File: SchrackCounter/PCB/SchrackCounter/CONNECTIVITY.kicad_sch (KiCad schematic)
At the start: 13 parts, among them J2 TYPE-C-31-M-12 (USB C CONN), U7 USBLC6-2SC6

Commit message: PCB layout update
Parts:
- added D_EXT1, D_EXT2, D_EXT3: Conn_01x02_Pin, Connector_JST:JST_XH_B2B-XH-A_1x02_P2.50mm_Vertical, symbol Connector:Conn_01x02_Pin
- added R2, R3, R4: 220R, Resistor_SMD:R_0805_2012Metric_Pad1.20x1.40mm_HandSolder, symbol Device:R
- added R5: 0R, Resistor_SMD:R_0805_2012Metric_Pad1.20x1.40mm_HandSolder, symbol Device:R
- renumbered D4 to D2, D5 to D3, D2 to D4, D3 to D5, R3 to R6, R4 to R7, R5 to R8, R2 to R9
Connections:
- net BZ1_PWM: now also R5.1; no longer BZ1.1 (+)
- net GND: now also D_EXT1.2 (Pin_2), D_EXT2.2 (Pin_2), D_EXT3.2 (Pin_2)
- new net: D_EXT1.1 (Pin_1), R2.1
- new net: BZ1.1 (+), R5.2
- new net: D_EXT3.1 (Pin_1), R4.1
- new net: D_EXT2.1 (Pin_1), R3.1
- new net LED_EXT1: R2.2
- new net LED_EXT2: R3.2
- new net LED_EXT3: R4.2
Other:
- note added: "EXTERNAL LEDS"
- note added: "LEDS/BUZZER"
- note removed: "SIGNALING"
- moved on the sheet: BZ1, D2, D3, D4, D5, R8, R9

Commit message: bom final, schematic updates
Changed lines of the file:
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@@
 		(dnp no)
 		(property "Reference" "R2"
-			(at 81.915 113.665 90)
+			(at 81.28 113.792 90)
 			(effects
 				(font
@@
 		(dnp no)
 		(property "Reference" "R3"
-			(at 81.915 126.365 90)
+			(at 81.28 126.492 90)
 			(effects
 				(font
@@
 		(dnp no)
 		(property "Reference" "R4"
-			(at 81.915 137.795 90)
-			(effects
-				(font
+			(at 81.28 137.922 90)
+			(effects
+				(font

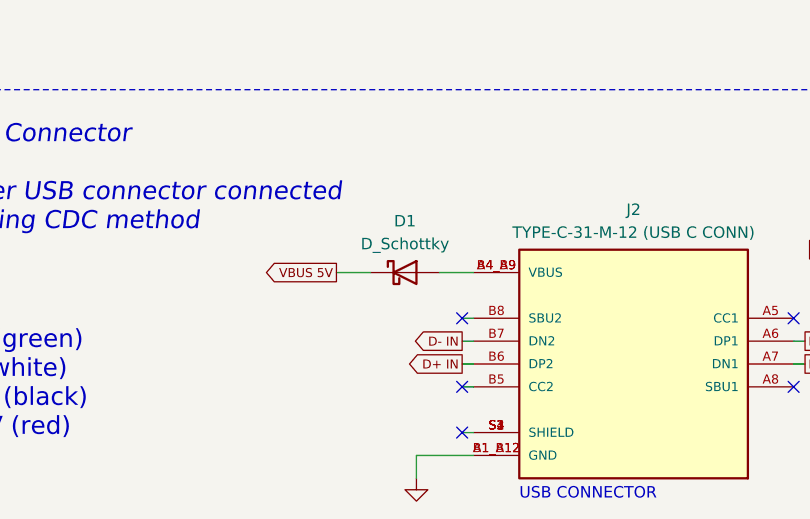
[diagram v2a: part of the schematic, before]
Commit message: PCB update, minor schematic update
PCB routing update, 7segment routing, and minor changes to the 7segments in schematic
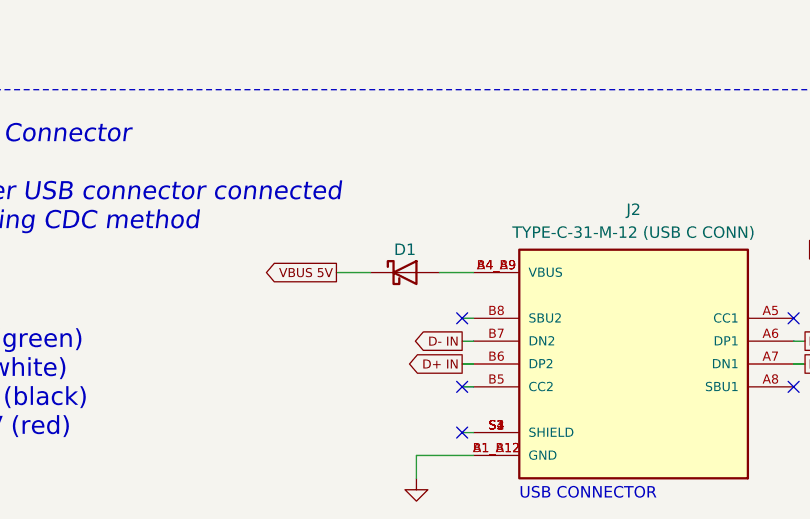
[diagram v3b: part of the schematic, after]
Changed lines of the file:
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@@
 		(effects
 			(font
+				(face "Bahnschrift")
 				(size 2 2)
 				(italic yes)
@@
 		(effects
 			(font
+				(face "Bahnschrift")
 				(size 5 5)
 				(thickness 1.2)
@@
 		(effects
 			(font
+				(face "Bahnschrift")
 				(size 5 5)
 				(thickness 1.2)
@@
 		(dnp no)
 		(property "Reference" "D1"
-			(at 120.65 46.355 0)
+			(at 120.65 49.53 0)
 			(effects
 				(font
@@
 					(size 1.27 1.27)
 				)
-			)
-		)
+				(hide yes)
+			)
+		)

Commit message: SchrackCounter
PCB Finished
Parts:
- renumbered D5 to D4, D4 to D5
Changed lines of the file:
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@@
 	(wire
 		(pts
-			(xy 124.46 52.07) (xy 128.27 52.07)
+			(xy 123.19 52.07) (xy 128.27 52.07)
 		)
 		(stroke
@@
 	(wire
 		(pts
-			(xy 113.03 52.07) (xy 116.84 52.07)
+			(xy 107.95 52.07) (xy 115.57 52.07)
 		)
 		(stroke
@@
 	(global_label "VBUS 5V"
 		(shape output)
-		(at 113.03 52.07 180)
+		(at 107.95 52.07 180)
 		(fields_autoplaced yes)
 		(effects
@@
 		)
 		(property "Intersheetrefs" "${INTERSHEET_REFS}"
-			(at 105.4326 52.07 0)
+			(at 100.3526 52.07 0)
 			(effects
 				(font
@@
 		(dnp no)
 		(fields_autoplaced yes)
-		(property "Reference" "#PWR023"
+		(property "Reference" "#PWR022"
 			(at 173.99 62.23 0)
 			(effects
@@
 			(project "SchrackCounter"
 				(path "/d96f2ffc-3f4c-4f71-b693-29f6b8c3245d/301b3ab9-8372-40d2-93c7-cd7607d23fc4"
-					(reference "#PWR023")
+					(reference "#PWR022")
 					(unit 1)
 				)
@@
 		(dnp no)
 		(fields_autoplaced yes)
-		(property "Reference" "#PWR026"
+		(property "Reference" "#PWR025"
 			(at 223.52 157.48 0)
 			(effects
@@
 			(project "SchrackCounter"
 				(path "/d96f2ffc-3f4c-4f71-b693-29f6b8c3245d/301b3ab9-8372-40d2-93c7-cd7607d23fc4"
-					(reference "#PWR026")
+					(reference "#PWR025")
 					(unit 1)
 				)
@@
 		(dnp no)
 		(fields_autoplaced yes)
-		(property "Reference" "#PWR021"
+		(property "Reference" "#PWR020"
 			(at 121.92 81.28 0)
 			(effects
@@
 			(project "SchrackCounter"
 				(path "/d96f2ffc-3f4c-4f71-b693-29f6b8c3245d/301b3ab9-8372-40d2-93c7-cd7607d23fc4"
-					(reference "#PWR021")
+					(reference "#PWR020")
 					(unit 1)
 				)
@@
 		(on_board yes)
 		(dnp no)
-		(property "Reference" "D4"
+		(property "Reference" "D5"
 			(at 215.9 142.24 0)
 			(effects
@@
 			(project "SchrackCounter"
 				(path "/d96f2ffc-3f4c-4f71-b693-29f6b8c3245d/301b3ab9-8372-40d2-93c7-cd7607d23fc4"
-					(reference "D4")
+					(reference "D5")
+					(unit 1)
+				)
+			)
+		)
+	)
+	(symbol
+		(lib_id "Device:D_Schottky")
+		(at 119.38 52.07 0)
+		(unit 1)
+		(exclude_from_sim no)
+		(in_bom yes)
+		(on_board yes)
+		(dnp no)
+		(property "Reference" "D1"
+			(at 119.38 48.895 0)
+			(effects
+				(font
+					(size 1.27 1.27)
+				)
+			)
+		)
+		(property "Value" "D_Schottky"
+			(at 119.38 46.99 0)
+			(effects
+				(font
+					(size 1.27 1.27)
+				)
+				(hide yes)
+			)
+		)
+		(property "Footprint" "Diode_SMD:D_1206_3216Metric_Pad1.42x1.75mm_HandSolder"
+			(at 119.38 52.07 0)
+			(effects
+				(font
+					(size 1.27 1.27)
+				)
+				(hide yes)
+			)
+		)
+		(property "Datasheet" "~"
+			(at 119.38 52.07 0)
+			(effects
+				(font
+					(size 1.27 1.27)
+				)
+				(hide yes)
+			)
+		)
+		(property "Description" "Schottky diode"
+			(at 119.38 52.07 0)
+			(effects
+				(font
+					(size 1.27 1.27)
+				)
+				(hide yes)
+			)
+		)
+		(pin "2"
+		)
+		(pin "1"
+		)
+		(instances
+			(project "SchrackCounter"
+				(path "/d96f2ffc-3f4c-4f71-b693-29f6b8c3245d/301b3ab9-8372-40d2-93c7-cd7607d23fc4"
+					(reference "D1")
 					(unit 1)
 				)
@@
 		(dnp no)
 		(fields_autoplaced yes)
-		(property "Reference" "#PWR022"
+		(property "Reference" "#PWR021"
 			(at 153.67 144.78 0)
 			(effects
@@
 			(project "SchrackCounter"
 				(path "/d96f2ffc-3f4c-4f71-b693-29f6b8c3245d/301b3ab9-8372-40d2-93c7-cd7607d23fc4"
-					(reference "#PWR022")
+					(reference "#PWR021")
 					(unit 1)
 				)
@@
 		(on_board yes)
 		(dnp no)
-		(property "Reference" "#PWR019"
+		(property "Reference" "#PWR018"
 			(at 87.63 139.7 0)
 			(effects
@@
 			(project "SchrackCounter"
 				(path "/d96f2ffc-3f4c-4f71-b693-29f6b8c3245d/301b3ab9-8372-40d2-93c7-cd7607d23fc4"
-					(reference "#PWR019")
+					(reference "#PWR018")
 					(unit 1)
 				)
@@
 		(on_board yes)
 		(dnp no)
-		(property "Reference" "#PWR018"
+		(property "Reference" "#PWR017"
 			(at 87.63 127 0)
 			(effects
@@
 			(project "SchrackCounter"
 				(path "/d96f2ffc-3f4c-4f71-b693-29f6b8c3245d/301b3ab9-8372-40d2-93c7-cd7607d23fc4"
-					(reference "#PWR018")
+					(reference "#PWR017")
 					(unit 1)
 				)
@@
 		(on_board yes)
 		(dnp no)
-		(property "Reference" "#PWR020"
+		(property "Reference" "#PWR019"
 			(at 87.63 151.13 0)
 			(effects
@@
 			(project "SchrackCounter"
 				(path "/d96f2ffc-3f4c-4f71-b693-29f6b8c3245d/301b3ab9-8372-40d2-93c7-cd7607d23fc4"
-					(reference "#PWR020")
-					(unit 1)
-				)
-			)
-		)
-	)
-	(symbol
-		(lib_id "Device:D_Schottky")
-		(at 120.65 52.07 0)
-		(unit 1)
-		(exclude_from_sim no)
-		(in_bom yes)
-		(on_board yes)
-		(dnp no)
-		(property "Reference" "D1"
-			(at 120.65 49.53 0)
-			(effects
-				(font
-					(size 1.27 1.27)
-				)
-			)
-		)
-		(property "Value" "D_Schottky"
-			(at 120.65 48.895 0)
-			(effects
-				(font
-					(size 1.27 1.27)
-				)
-				(hide yes)
-			)
-		)
-		(property "Footprint" "Diode_SMD:D_1206_3216Metric_Pad1.42x1.75mm_HandSolder"
-			(at 120.65 52.07 0)
-			(effects
-				(font
-					(size 1.27 1.27)
-				)
-				(hide yes)
-			)
-		)
-		(property "Datasheet" "~"
-			(at 120.65 52.07 0)
-			(effects
-				(font
-					(size 1.27 1.27)
-				)
-				(hide yes)
-			)
-		)
-		(property "Description" "Schottky diode"
-			(at 120.65 52.07 0)
-			(effects
-				(font
-					(size 1.27 1.27)
-				)
-				(hide yes)
-			)
-		)
-		(pin "2"
-		)
-		(pin "1"
-		)
-		(instances
-			(project "SchrackCounter"
-				(path "/d96f2ffc-3f4c-4f71-b693-29f6b8c3245d/301b3ab9-8372-40d2-93c7-cd7607d23fc4"
-					(reference "D1")
+					(reference "#PWR019")
 					(unit 1)
 				)
@@
 		(dnp no)
 		(property "Reference" "R2"
-			(at 81.28 113.792 90)
+			(at 82.55 113.665 90)
 			(effects
 				(font
@@
 		(dnp no)
 		(property "Reference" "R3"
-			(at 81.28 126.492 90)
+			(at 82.55 126.365 90)
 			(effects
 				(font
@@
 		(dnp no)
 		(fields_autoplaced yes)
-		(property "Reference" "#PWR025"
+		(property "Reference" "#PWR023"
 			(at 223.52 76.2 0)
 			(effects
@@
 			(project "SchrackCounter"
 				(path "/d96f2ffc-3f4c-4f71-b693-29f6b8c3245d/301b3ab9-8372-40d2-93c7-cd7607d23fc4"
-					(reference "#PWR025")
+					(reference "#PWR023")
 					(unit 1)
 				)
@@
 		(on_board yes)
 		(dnp no)
-		(property "Reference" "D5"
+		(property "Reference" "D4"
 			(at 215.9 132.08 0)
 			(effects
@@
 			(project "SchrackCounter"
 				(path "/d96f2ffc-3f4c-4f71-b693-29f6b8c3245d/301b3ab9-8372-40d2-93c7-cd7607d23fc4"
-					(reference "D5")
+					(reference "D4")
 					(unit 1)
 				)
@@
 		(dnp no)
 		(property "Reference" "R4"
-			(at 81.28 137.922 90)
+			(at 82.55 137.795 90)
 			(effects
 				(font

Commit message: fixes to be made
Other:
- moved on the sheet: D1
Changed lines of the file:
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@@
 	(wire
 		(pts
-			(xy 123.19 52.07) (xy 128.27 52.07)
+			(xy 125.73 52.07) (xy 128.27 52.07)
 		)
 		(stroke
@@
 	(wire
 		(pts
-			(xy 107.95 52.07) (xy 115.57 52.07)
+			(xy 114.3 52.07) (xy 118.11 52.07)
 		)
 		(stroke
@@
 	(global_label "VBUS 5V"
 		(shape output)
-		(at 107.95 52.07 180)
+		(at 114.3 52.07 180)
 		(fields_autoplaced yes)
 		(effects
@@
 		)
 		(property "Intersheetrefs" "${INTERSHEET_REFS}"
-			(at 100.3526 52.07 0)
+			(at 106.7026 52.07 0)
 			(effects
 				(font
@@
 	(symbol
 		(lib_id "Device:D_Schottky")
-		(at 119.38 52.07 0)
+		(at 121.92 52.07 0)
 		(unit 1)
 		(exclude_from_sim no)
@@
 		(dnp no)
 		(property "Reference" "D1"
-			(at 119.38 48.895 0)
+			(at 121.92 48.895 0)
 			(effects
 				(font
@@
 		)
 		(property "Value" "D_Schottky"
-			(at 119.38 46.99 0)
+			(at 121.92 46.99 0)
 			(effects
 				(font
@@
 		)
 		(property "Footprint" "Diode_SMD:D_1206_3216Metric_Pad1.42x1.75mm_HandSolder"
-			(at 119.38 52.07 0)
+			(at 121.92 52.07 0)
 			(effects
 				(font
@@
 		)
 		(property "Datasheet" "~"
-			(at 119.38 52.07 0)
+			(at 121.92 52.07 0)
 			(effects
 				(font
@@
 		)
 		(property "Description" "Schottky diode"
-			(at 119.38 52.07 0)
-			(effects
-				(font
+			(at 121.92 52.07 0)
+			(effects
+				(font

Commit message: PCB update
pcb redesign
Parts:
- added D2, D3: LED, LED_SMD:LED_0805_2012Metric_Pad1.15x1.40mm_HandSolder, symbol Device:LED
- added R6, R7: 220R, Resistor_SMD:R_0805_2012Metric_Pad1.20x1.40mm_HandSolder, symbol Device:R
- renumbered D2 to D4, D3 to D5, D4 to D6, D5 to D7, J2 to J1, R8 to R10, R9 to R11, R6 to R8, R7 to R9
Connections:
- net GND: now also D2.1 (K), D3.1 (K)
- new net: D2.2 (A), R6.2
- new net: D3.2 (A), R7.2
- new net +3V3: R6.1
- new net VBATT: R7.1
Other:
- moved on the sheet: BZ1, R5

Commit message: PCB finalizing
Final routing and layout
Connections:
- net +3V3: now also D2.2 (A); no longer R6.1
- net GND: now also R6.2, R7.2; no longer D2.1 (K), D3.1 (K)
- net VBATT: now also D3.2 (A); no longer R7.1
- new net: D3.1 (K), R7.1
- new net: D2.1 (K), R6.1
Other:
- moved on the sheet: D2, D3
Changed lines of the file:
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@@
 	(wire
 		(pts
-			(xy 176.53 129.54) (xy 172.72 129.54)
+			(xy 176.53 129.54) (xy 173.99 129.54)
 		)
 		(stroke
@@
 	(wire
 		(pts
+			(xy 166.37 118.11) (xy 163.83 118.11)
+		)
+		(stroke
+			(width 0)
+			(type default)
+		)
+	)
+	(wire
+		(pts
 			(xy 223.52 147.32) (xy 223.52 151.13)
 		)
@@
 	(wire
 		(pts
+			(xy 166.37 129.54) (xy 163.83 129.54)
+		)
+		(stroke
+			(width 0)
+			(type default)
+		)
+	)
+	(wire
+		(pts
 			(xy 208.28 123.19) (xy 212.09 123.19)
 		)
@@
 	(wire
 		(pts
-			(xy 176.53 118.11) (xy 172.72 118.11)
+			(xy 176.53 118.11) (xy 173.99 118.11)
 		)
 		(stroke
@@
 	(wire
 		(pts
-			(xy 163.83 118.11) (xy 165.1 118.11)
-		)
-		(stroke
-			(width 0)
-			(type default)
-		)
-	)
-	(wire
-		(pts
-			(xy 163.83 129.54) (xy 165.1 129.54)
-		)
-		(stroke
-			(width 0)
-			(type default)
-		)
-	)
-	(wire
-		(pts
 			(xy 88.9 130.81) (xy 86.36 130.81)
 		)
@@
 	)
 	(symbol
-		(lib_id "Device:R")
-		(at 160.02 118.11 90)
-		(unit 1)
-		(exclude_from_sim no)
-		(in_bom yes)
-		(on_board yes)
-		(dnp no)
-		(property "Reference" "R6"
-			(at 160.02 113.665 90)
-			(effects
-				(font
-					(size 1.27 1.27)
-				)
-			)
-		)
-		(property "Value" "220R"
-			(at 160.02 115.57 90)
-			(effects
-				(font
-					(size 1.27 1.27)
-				)
-			)
-		)
-		(property "Footprint" "Resistor_SMD:R_0805_2012Metric_Pad1.20x1.40mm_HandSolder"
-			(at 160.02 119.888 90)
-			(effects
-				(font
-					(size 1.27 1.27)
-				)
-				(hide yes)
-			)
-		)
-		(property "Datasheet" "~"
-			(at 160.02 118.11 0)
-			(effects
-				(font
-					(size 1.27 1.27)
-				)
-				(hide yes)
-			)
-		)
-		(property "Description" "Resistor"
-			(at 160.02 118.11 0)
-			(effects
-				(font
-					(size 1.27 1.27)
-				)
-				(hide yes)
-			)
-		)
-		(pin "2"
-		)
-		(pin "1"
-		)
-		(instances
-			(project "SchrackCounter"
-				(path "/d96f2ffc-3f4c-4f71-b693-29f6b8c3245d/301b3ab9-8372-40d2-93c7-cd7607d23fc4"
-					(reference "R6")
-					(unit 1)
-				)
-			)
-		)
-	)
-	(symbol
 		(lib_id "Device:Buzzer")
 		(at 137.16 124.46 90)
@@
 	(symbol
 		(lib_id "Device:LED")
-		(at 168.91 129.54 180)
+		(at 160.02 129.54 180)
 		(unit 1)
 		(exclude_from_sim no)
@@
 		(dnp no)
 		(property "Reference" "D3"
-			(at 168.91 124.46 0)
+			(at 160.02 124.46 0)
 			(effects
 				(font
@@
 		)
 		(property "Value" "LED"
-			(at 168.91 126.365 0)
+			(at 160.02 126.365 0)
 			(effects
 				(font
@@
 		)
 		(property "Footprint" "LED_SMD:LED_0805_2012Metric_Pad1.15x1.40mm_HandSolder"
-			(at 168.91 129.54 0)
+			(at 160.02 129.54 0)
 			(effects
 				(font
@@
 		)
 		(property "Datasheet" "~"
-			(at 168.91 129.54 0)
+			(at 160.02 129.54 0)
 			(effects
 				(font
@@
 		)
 		(property "Description" "Light emitting diode"
-			(at 168.91 129.54 0)
+			(at 160.02 129.54 0)
 			(effects
 				(font
@@
 	)
 	(symbol
-		(lib_id "Device:R")
-		(at 160.02 129.54 90)
-		(unit 1)
-		(exclude_from_sim no)
-		(in_bom yes)
-		(on_board yes)
-		(dnp no)
-		(property "Reference" "R7"
-			(at 160.02 125.095 90)
-			(effects
-				(font
-					(size 1.27 1.27)
-				)
-			)
-		)
-		(property "Value" "220R"
-			(at 160.02 127 90)
-			(effects
-				(font
-					(size 1.27 1.27)
-				)
-			)
-		)
-		(property "Footprint" "Resistor_SMD:R_0805_2012Metric_Pad1.20x1.40mm_HandSolder"
-			(at 160.02 131.318 90)
-			(effects
-				(font
-					(size 1.27 1.27)
-				)
-				(hide yes)
-			)
-		)
-		(property "Datasheet" "~"
-			(at 160.02 129.54 0)
-			(effects
-				(font
-					(size 1.27 1.27)
-				)
-				(hide yes)
-			)
-		)
-		(property "Description" "Resistor"
-			(at 160.02 129.54 0)
-			(effects
-				(font
-					(size 1.27 1.27)
-				)
-				(hide yes)
-			)
-		)
-		(pin "2"
-		)
-		(pin "1"
-		)
-		(instances
-			(project "SchrackCounter"
-				(path "/d96f2ffc-3f4c-4f71-b693-29f6b8c3245d/301b3ab9-8372-40d2-93c7-cd7607d23fc4"
-					(reference "R7")
-					(unit 1)
-				)
-			)
-		)
-	)
-	(symbol
 		(lib_id "power:GND")
 		(at 176.53 118.11 0)
@@
 	)
 	(symbol
+		(lib_id "Device:R")
+		(at 170.18 118.11 90)
+		(unit 1)
+		(exclude_from_sim no)
+		(in_bom yes)
+		(on_board yes)
+		(dnp no)
+		(property "Reference" "R6"
+			(at 170.18 113.665 90)
+			(effects
+				(font
+					(size 1.27 1.27)
+				)
+			)
+		)
+		(property "Value" "220R"
+			(at 170.18 115.57 90)
+			(effects
+				(font
+					(size 1.27 1.27)
+				)
+			)
+		)
+		(property "Footprint" "Resistor_SMD:R_0805_2012Metric_Pad1.20x1.40mm_HandSolder"
+			(at 170.18 119.888 90)
+			(effects
+				(font
+					(size 1.27 1.27)
+				)
+				(hide yes)
+			)
+		)
+		(property "Datasheet" "~"
+			(at 170.18 118.11 0)
+			(effects
+				(font
+					(size 1.27 1.27)
+				)
+				(hide yes)
+			)
+		)
+		(property "Description" "Resistor"
+			(at 170.18 118.11 0)
+			(effects
+				(font
+					(size 1.27 1.27)
+				)
+				(hide yes)
+			)
+		)
+		(pin "2"
+		)
+		(pin "1"
+		)
+		(instances
+			(project "SchrackCounter"
+				(path "/d96f2ffc-3f4c-4f71-b693-29f6b8c3245d/301b3ab9-8372-40d2-93c7-cd7607d23fc4"
+					(reference "R6")
+					(unit 1)
+				)
+			)
+		)
+	)
+	(symbol
 		(lib_id "Device:LED")
 		(at 215.9 113.03 180)
@@
 	(symbol
 		(lib_id "Device:LED")
-		(at 168.91 118.11 180)
+		(at 160.02 118.11 180)
 		(unit 1)
 		(exclude_from_sim no)
@@
 		(dnp no)
 		(property "Reference" "D2"
-			(at 168.91 113.03 0)
+			(at 160.02 113.03 0)
 			(effects
 				(font
@@
 		)
 		(property "Value" "LED"
-			(at 168.91 114.935 0)
+			(at 160.02 114.935 0)
 			(effects
 				(font
@@
 		)
 		(property "Footprint" "LED_SMD:LED_0805_2012Metric_Pad1.15x1.40mm_HandSolder"
-			(at 168.91 118.11 0)
+			(at 160.02 118.11 0)
 			(effects
 				(font
@@
 		)
 		(property "Datasheet" "~"
-			(at 168.91 118.11 0)
+			(at 160.02 118.11 0)
 			(effects
 				(font
@@
 		)
 		(property "Description" "Light emitting diode"
-			(at 168.91 118.11 0)
+			(at 160.02 118.11 0)
 			(effects
 				(font
@@
 					(unit 1)
 				)
+			)
+		)
+	)
+	(symbol
+		(lib_id "Device:R")
+		(at 170.18 129.54 90)
+		(unit 1)
+		(exclude_from_sim no)
+		(in_bom yes)
+		(on_board yes)
+		(dnp no)
+		(property "Reference" "R7"
+			(at 170.18 125.095 90)
+			(effects
+				(font
+					(size 1.27 1.27)
+				)
+			)
+		)
+		(property "Value" "220R"
+			(at 170.18 127 90)
+			(effects
+				(font
+					(size 1.27 1.27)
+				)
+			)
+		)
+		(property "Footprint" "Resistor_SMD:R_0805_2012Metric_Pad1.20x1.40mm_HandSolder"
+			(at 170.18 131.318 90)
+			(effects
+				(font
+					(size 1.27 1.27)
+				)
+				(hide yes)
+			)
+		)
+		(property "Datasheet" "~"
+			(at 170.18 129.54 0)
+			(effects
+				(font
+					(size 1.27 1.27)
+				)
+				(hide yes)
+			)
+		)
+		(property "Description" "Resistor"
+			(at 170.18 129.54 0)
+			(effects
+				(font
+					(size 1.27 1.27)
+				)
+				(hide yes)
+			)
+		)
+		(pin "2"
+		)
+		(pin "1"
+		)
+		(instances
+			(project "SchrackCounter"
+				(path "/d96f2ffc-3f4c-4f71-b693-29f6b8c3245d/301b3ab9-8372-40d2-93c7-cd7607d23fc4"
+					(reference "R7")
+					(unit 1)
+				)
